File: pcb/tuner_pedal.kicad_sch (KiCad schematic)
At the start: 43 parts, among them U1 STM32F411CEUx, U2 PCM1802DB, U3 MCP1700T-3302E/TT, U4 TPS54302, X1 ECS-2520MVLC-081.92, Y1 25MHz 9pF

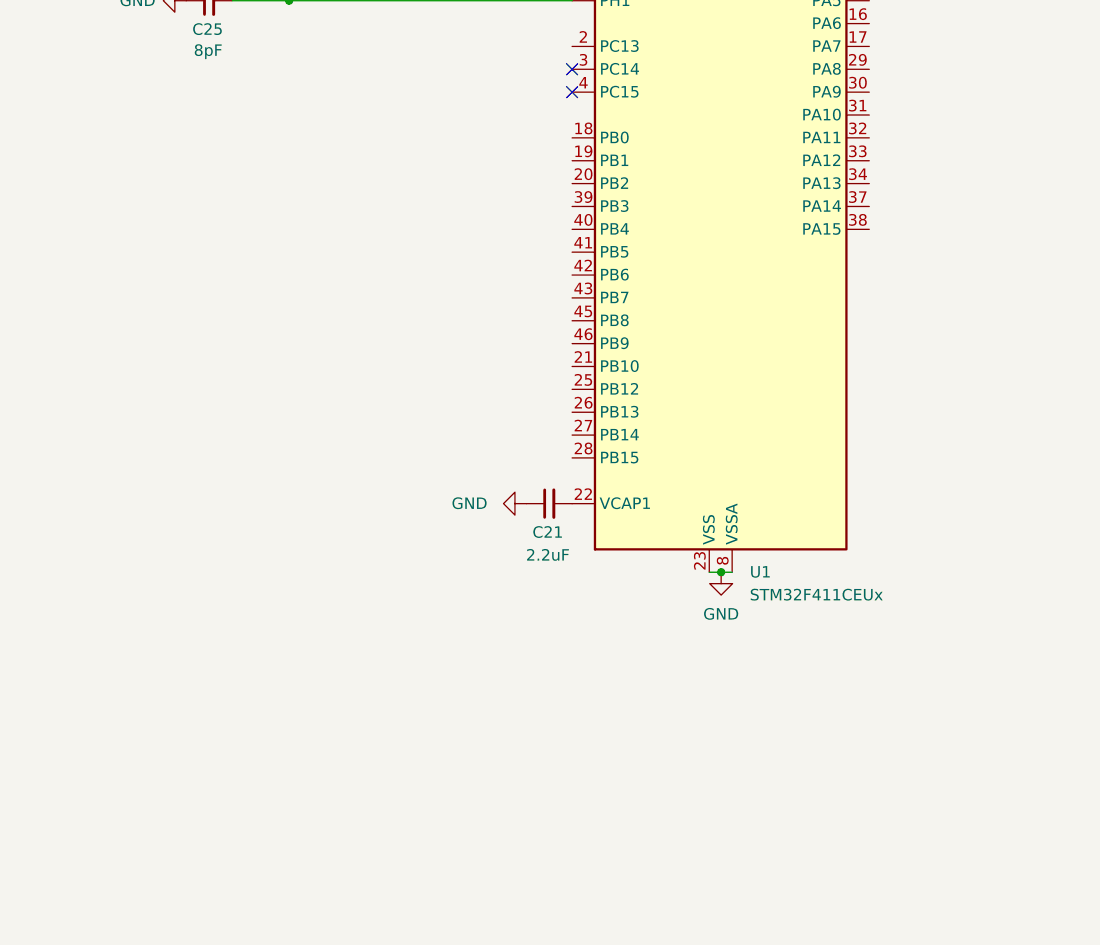
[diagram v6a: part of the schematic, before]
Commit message: Added SWD header
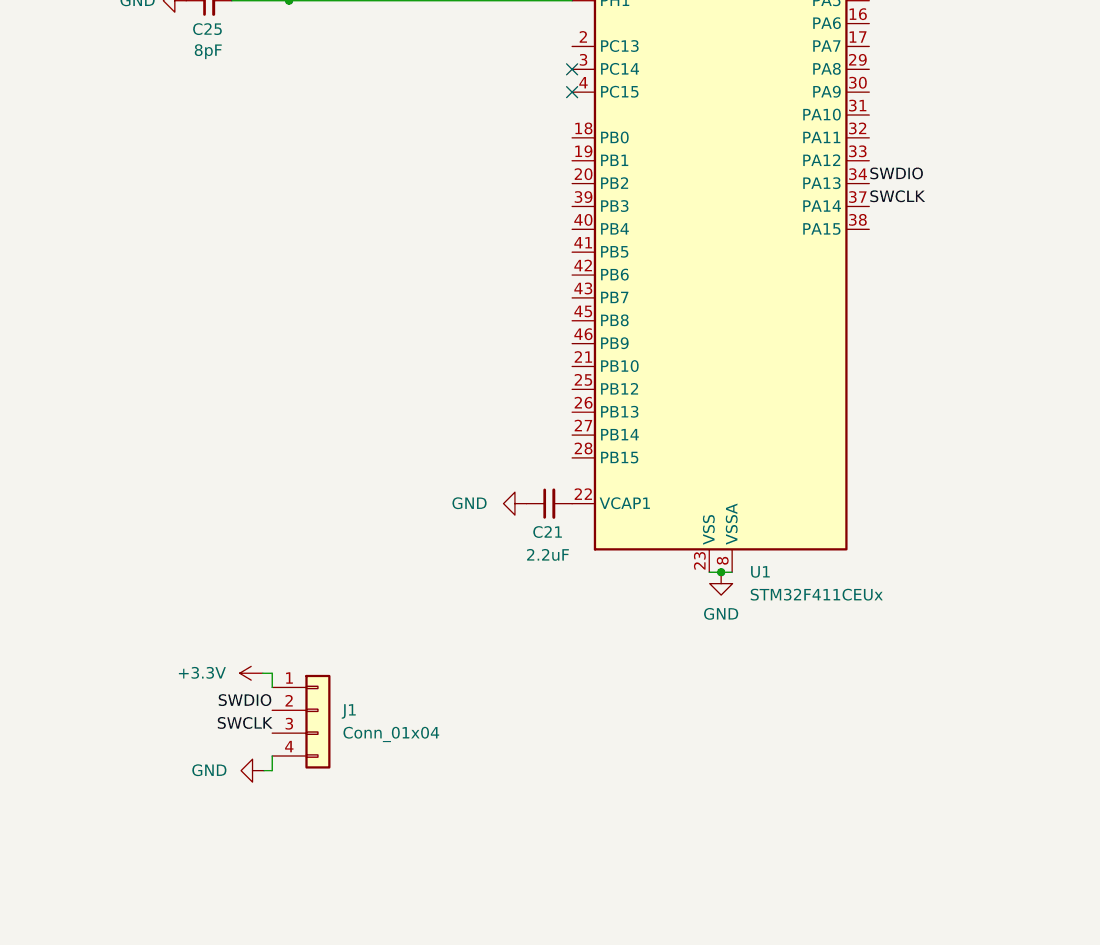
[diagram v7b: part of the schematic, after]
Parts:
- added J1: Conn_01x04, Connector_PinHeader_2.54mm:PinHeader_1x04_P2.54mm_Vertical, symbol Connector_Generic:Conn_01x04
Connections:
- net +3.3V: now also J1.1 (Pin_1)
- net GND: now also J1.4 (Pin_4)
- net SWDIO: now reaches U1.34 (PA13)
- net SWDIO: now also J1.2 (Pin_2)
- net SWCLK: now reaches U1.37 (PA14)
- net SWCLK: now also J1.3 (Pin_3)
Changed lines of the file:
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@@
+    (stroke (width 0) (type default))
+  )
+  (wire (pts (xy 157.734 119.5832) (xy 157.734 121.158))
     (stroke (width 0) (type default))
   )
@@
     (stroke (width 0) (type default))
   )
+  (wire (pts (xy 156.8196 130.4036) (xy 157.734 130.4036))
+    (stroke (width 0) (type default))
+  )
   (wire (pts (xy 74.0156 165.5064) (xy 74.0664 165.5064))
     (stroke (width 0) (type default))
@@
     (stroke (width 0) (type default))
   )
+  (wire (pts (xy 156.6672 119.5832) (xy 157.734 119.5832))
+    (stroke (width 0) (type default))
+  )
   (wire (pts (xy 23.622 41.656) (xy 23.622 43.688))
     (stroke (width 0) (type default))
@@
   )
   (wire (pts (xy 173.8884 42.3164) (xy 191.0588 42.3164))
+    (stroke (width 0) (type default))
+  )
+  (wire (pts (xy 157.734 130.4036) (xy 157.734 128.778))
     (stroke (width 0) (type default))
   )
@@
     (effects (font (size 1.27 1.27)) (justify left bottom))
   )
+  (label "SWDIO" (at 157.734 123.698 180) (fields_autoplaced)
+    (effects (font (size 1.27 1.27)) (justify right bottom))
+  )
+  (label "SWCLK" (at 157.734 126.238 180) (fields_autoplaced)
+    (effects (font (size 1.27 1.27)) (justify right bottom))
+  )
   (label "SCKI" (at 52.1208 66.294 0) (fields_autoplaced)
     (effects (font (size 1.27 1.27)) (justify left bottom))
   )
+  (label "SWCLK" (at 224.0788 67.7164 0) (fields_autoplaced)
+    (effects (font (size 1.27 1.27)) (justify left bottom))
+  )
   (label "buffered_in" (at 59.8424 120.7516 0) (fields_autoplaced)
     (effects (font (size 1.27 1.27)) (justify left bottom))
   )
+  (label "SWDIO" (at 224.0788 65.1764 0) (fields_autoplaced)
+    (effects (font (size 1.27 1.27)) (justify left bottom))
+  )
   (label "SCKI" (at 56.8452 174.1932 0) (fields_autoplaced)
     (effects (font (size 1.27 1.27)) (justify left bottom))
@@
         (path "/be09f3cc-c79c-49de-93a4-4a01bf6bfbcf"
           (reference "C10") (unit 1)
+        )
+      )
+    )
+  )
+  (symbol (lib_id "power:+3.3V") (at 156.6672 119.5832 90) (unit 1)
+    (in_bom yes) (on_board yes) (dnp no) (fields_autoplaced)
+    (property "Reference" "#PWR034" (at 160.4772 119.5832 0)
+      (effects (font (size 1.27 1.27)) hide)
+    )
+    (property "Value" "+3.3V" (at 152.6032 119.5832 90)
+      (effects (font (size 1.27 1.27)) (justify left))
+    )
+    (property "Footprint" "" (at 156.6672 119.5832 0)
+      (effects (font (size 1.27 1.27)) hide)
+    )
+    (property "Datasheet" "" (at 156.6672 119.5832 0)
+      (effects (font (size 1.27 1.27)) hide)
+    )
+    (pin "1")
+    (instances
+      (project "tuner_pedal"
+        (path "/be09f3cc-c79c-49de-93a4-4a01bf6bfbcf"
+          (reference "#PWR034") (unit 1)
         )
       )
@@
     )
   )
+  (symbol (lib_id "power:GND") (at 156.8196 130.4036 270) (unit 1)
+    (in_bom yes) (on_board yes) (dnp no) (fields_autoplaced)
+    (property "Reference" "#PWR035" (at 150.4696 130.4036 0)
+      (effects (font (size 1.27 1.27)) hide)
+    )
+    (property "Value" "GND" (at 152.7556 130.4036 90)
+      (effects (font (size 1.27 1.27)) (justify right))
+    )
+    (property "Footprint" "" (at 156.8196 130.4036 0)
+      (effects (font (size 1.27 1.27)) hide)
+    )
+    (property "Datasheet" "" (at 156.8196 130.4036 0)
+      (effects (font (size 1.27 1.27)) hide)
+    )
+    (pin "1")
+    (instances
+      (project "tuner_pedal"
+        (path "/be09f3cc-c79c-49de-93a4-4a01bf6bfbcf"
+          (reference "#PWR035") (unit 1)
+        )
+      )
+    )
+  )
   (symbol (lib_id "power:GND") (at 96.52 54.864 0) (unit 1)
     (in_bom yes) (on_board yes) (dnp no) (fields_autoplaced)
@@
         )
       )
+    )
+  )
+  (symbol (lib_id "Connector_Generic:Conn_01x04") (at 162.814 123.698 0) (unit 1)
+    (in_bom yes) (on_board yes) (dnp no) (fields_autoplaced)
+    (property "Reference" "J1" (at 165.5572 123.698 0)
+      (effects (font (size 1.27 1.27)) (justify left))
+    )
+    (property "Value" "Conn_01x04" (at 165.5572 126.238 0)
+      (effects (font (size 1.27 1.27)) (justify left))
+    )
+    (property "Footprint" "Connector_PinHeader_2.54mm:PinHeader_1x04_P2.54mm_Vertical" (at 162.814 123.698 0)
+      (effects (font (size 1.27 1.27)) hide)
+    )
+    (property "Datasheet" "~" (at 162.814 123.698 0)
+      (effects (font (size 1.27 1.27)) hide)
+    )
+    (pin "1")
+    (pin "2")
+    (pin "3")
+    (pin "4")
+    (instances
+      (project "tuner_pedal"
+        (path "/be09f3cc-c79c-49de-93a4-4a01bf6bfbcf"
+          (reference "J1") (unit 1)
+        )
+      )
